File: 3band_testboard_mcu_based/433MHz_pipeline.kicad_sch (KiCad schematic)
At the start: 13 parts, among them J1 Conn_Coaxial, U1 RFM96W-433S2

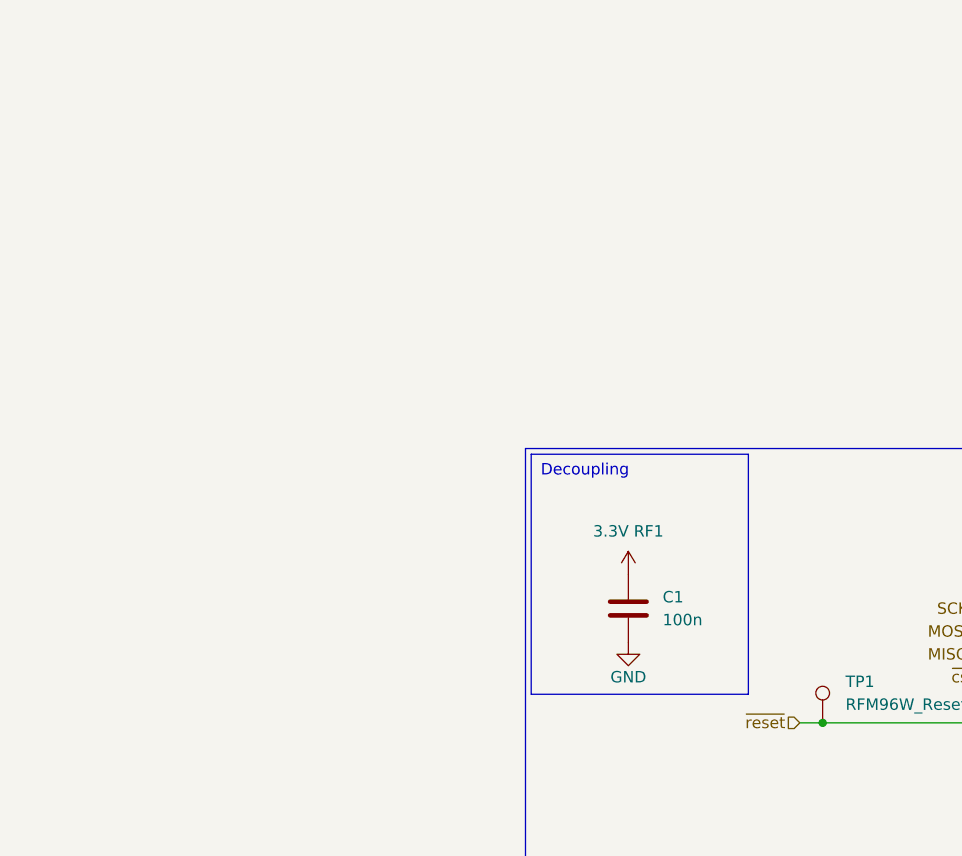
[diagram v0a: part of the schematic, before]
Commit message: Færdiggjorde GPIO
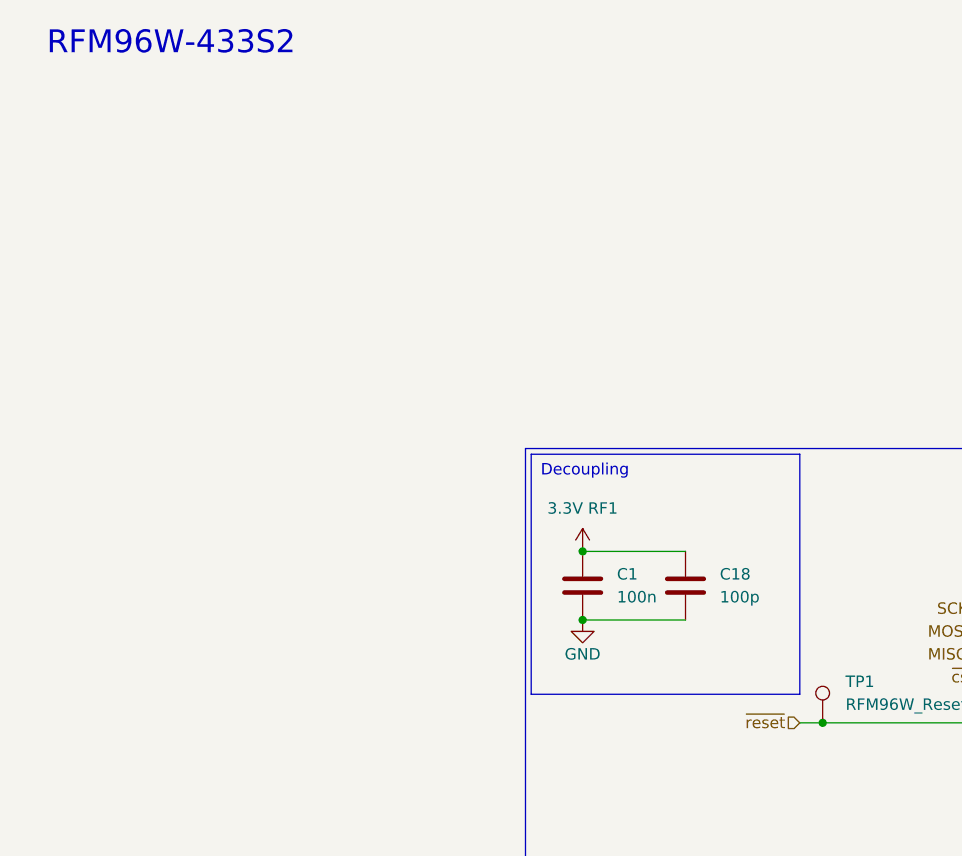
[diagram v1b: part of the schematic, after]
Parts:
- added C18: 100p, Capacitor_SMD:C_0603_1608Metric_Pad1.08x0.95mm_HandSolder, symbol Device:C
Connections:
- net 3.3V RF1: now also C18.1
- net GND: now also C18.2
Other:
- note added: "RFM96W-433S2"
- company: (none) -> AAU-connectivity
- title: (none) -> 3-band-LoRa testboard
- moved on the sheet: C1
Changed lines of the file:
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@@
 	(generator_version "9.0")
 	(paper "A4")
+	(title_block
+		(title "3-band-LoRa testboard")
+		(date "2025-30-03")
+		(rev "1")
+		(company "AAU-connectivity")
+		(comment 1 "Malthe Sennels")
+	)
 	(rectangle
 		(start 69.85 60.96)
@@
 	(rectangle
 		(start 70.485 61.595)
-		(end 94.615 88.265)
+		(end 100.33 88.265)
 		(stroke
 			(width 0)
@@
 		(fill
 			(type none)
+		)
+	)
+	(text "RFM96W-433S2"
+		(exclude_from_sim no)
+		(at 30.48 16.002 0)
+		(effects
+			(font
+				(size 2.54 2.54)
+			)
 		)
 	)
@@
 	)
 	(junction
+		(at 76.2 72.39)
+		(diameter 0)
+		(color 0 0 0 0)
+	)
+	(junction
 		(at 102.87 91.44)
 		(diameter 0)
@@
 	)
 	(junction
+		(at 76.2 80.01)
+		(diameter 0)
+		(color 0 0 0 0)
+	)
+	(junction
 		(at 138.43 101.6)
 		(diameter 0)
@@
 	(wire
 		(pts
+			(xy 76.2 80.01) (xy 87.63 80.01)
+		)
+		(stroke
+			(width 0)
+			(type default)
+		)
+	)
+	(wire
+		(pts
 			(xy 181.61 78.74) (xy 182.88 78.74)
 		)
@@
 		(pts
 			(xy 120.65 78.74) (xy 125.73 78.74)
+		)
+		(stroke
+			(width 0)
+			(type default)
+		)
+	)
+	(wire
+		(pts
+			(xy 76.2 72.39) (xy 87.63 72.39)
 		)
 		(stroke
@@
 	(symbol
 		(lib_id "power:+3.3V")
-		(at 81.28 74.93 0)
+		(at 76.2 72.39 0)
 		(unit 1)
 		(exclude_from_sim no)
@@
 		(fields_autoplaced yes)
 		(property "Reference" "#PWR043"
-			(at 81.28 78.74 0)
+			(at 76.2 76.2 0)
 			(effects
 				(font
@@
 		)
 		(property "Value" "3.3V RF1"
-			(at 81.28 70.1543 0)
+			(at 76.2 67.6143 0)
 			(effects
 				(font
@@
 		)
 		(property "Footprint" ""
-			(at 81.28 74.93 0)
+			(at 76.2 72.39 0)
 			(effects
 				(font
@@
 		)
 		(property "Datasheet" ""
-			(at 81.28 74.93 0)
+			(at 76.2 72.39 0)
 			(effects
 				(font
@@
 		)
 		(property "Description" "Power symbol creates a global label with name \"+3.3V\""
-			(at 81.28 74.93 0)
+			(at 76.2 72.39 0)
 			(effects
 				(font
@@
 				(path "/65994ec6-42d7-4e39-8f54-f3ae991c25e9/10123ff1-9060-4000-8c60-359bb6febe8f"
 					(reference "#PWR043")
+					(unit 1)
+				)
+			)
+		)
+	)
+	(symbol
+		(lib_id "Device:C")
+		(at 87.63 76.2 0)
+		(unit 1)
+		(exclude_from_sim no)
+		(in_bom yes)
+		(on_board yes)
+		(dnp no)
+		(fields_autoplaced yes)
+		(property "Reference" "C18"
+			(at 91.44 74.9299 0)
+			(effects
+				(font
+					(size 1.27 1.27)
+				)
+				(justify left)
+			)
+		)
+		(property "Value" "100p"
+			(at 91.44 77.4699 0)
+			(effects
+				(font
+					(size 1.27 1.27)
+				)
+				(justify left)
+			)
+		)
+		(property "Footprint" "Capacitor_SMD:C_0603_1608Metric_Pad1.08x0.95mm_HandSolder"
+			(at 88.5952 80.01 0)
+			(effects
+				(font
+					(size 1.27 1.27)
+				)
+				(hide yes)
+			)
+		)
+		(property "Datasheet" "~"
+			(at 87.63 76.2 0)
+			(effects
+				(font
+					(size 1.27 1.27)
+				)
+				(hide yes)
+			)
+		)
+		(property "Description" "Unpolarized capacitor"
+			(at 87.63 76.2 0)
+			(effects
+				(font
+					(size 1.27 1.27)
+				)
+				(hide yes)
+			)
+		)
+		(pin "1"
+		)
+		(pin "2"
+		)
+		(instances
+			(project "3band_testboard_mcu_based"
+				(path "/65994ec6-42d7-4e39-8f54-f3ae991c25e9/10123ff1-9060-4000-8c60-359bb6febe8f"
+					(reference "C18")
 					(unit 1)
 				)
@@
 	(symbol
 		(lib_id "power:GND")
-		(at 81.28 82.55 0)
+		(at 76.2 80.01 0)
 		(unit 1)
 		(exclude_from_sim no)
@@
 		(dnp no)
 		(property "Reference" "#PWR04"
-			(at 81.28 88.9 0)
+			(at 76.2 86.36 0)
 			(effects
 				(font
@@
 		)
 		(property "Value" "GND"
-			(at 81.28 86.36 0)
+			(at 76.2 83.82 0)
 			(effects
 				(font
@@
 		)
 		(property "Footprint" ""
-			(at 81.28 82.55 0)
+			(at 76.2 80.01 0)
 			(effects
 				(font
@@
 		)
 		(property "Datasheet" ""
-			(at 81.28 82.55 0)
+			(at 76.2 80.01 0)
 			(effects
 				(font
@@
 		)
 		(property "Description" "Power symbol creates a global label with name \"GND\" , ground"
-			(at 81.28 82.55 0)
+			(at 76.2 80.01 0)
 			(effects
 				(font
@@
 	(symbol
 		(lib_id "Device:C")
-		(at 81.28 78.74 0)
+		(at 76.2 76.2 0)
 		(unit 1)
 		(exclude_from_sim no)
@@
 		(fields_autoplaced yes)
 		(property "Reference" "C1"
-			(at 85.09 77.4699 0)
+			(at 80.01 74.9299 0)
 			(effects
 				(font
@@
 		)
 		(property "Value" "100n"
-			(at 85.09 80.0099 0)
+			(at 80.01 77.4699 0)
 			(effects
 				(font
@@
 		)
 		(property "Footprint" "Capacitor_SMD:C_0603_1608Metric_Pad1.08x0.95mm_HandSolder"
-			(at 82.2452 82.55 0)
+			(at 77.1652 80.01 0)
 			(effects
 				(font
@@
 		)
 		(property "Datasheet" "~"
-			(at 81.28 78.74 0)
+			(at 76.2 76.2 0)
 			(effects
 				(font
@@
 		)
 		(property "Description" "Unpolarized capacitor"
-			(at 81.28 78.74 0)
-			(effects
-				(font
+			(at 76.2 76.2 0)
+			(effects
+				(font

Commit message: DRC check, and price
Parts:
- J1: footprint Connector_Coaxial:SMA_Amphenol_132289_EdgeMount -> Connector_Coaxial:SMA_Samtec_SMA-J-P-H-ST-EM1_EdgeMount
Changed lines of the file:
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@@
 			)
 		)
-		(property "Footprint" "Connector_Coaxial:SMA_Amphenol_132289_EdgeMount"
+		(property "Footprint" "Connector_Coaxial:SMA_Samtec_SMA-J-P-H-ST-EM1_EdgeMount"
 			(at 232.41 78.74 0)
 			(effects
